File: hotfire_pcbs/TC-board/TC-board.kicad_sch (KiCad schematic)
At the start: 14 parts, among them J1 JST, J2 JST, J3 PCIE-LP-01-01-F-DV-A-TR, U1 MAX31856_Breakout, U2 MAX31856_Breakout

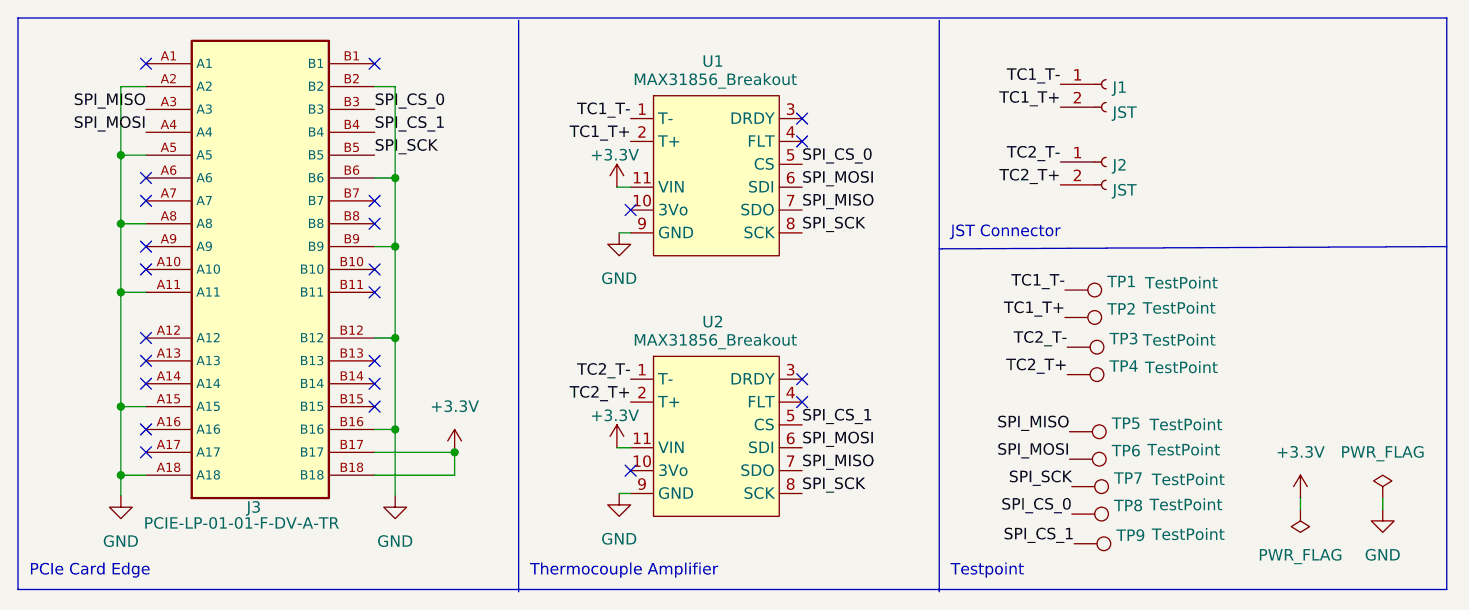
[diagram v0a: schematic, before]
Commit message: Changed JST to DSUB
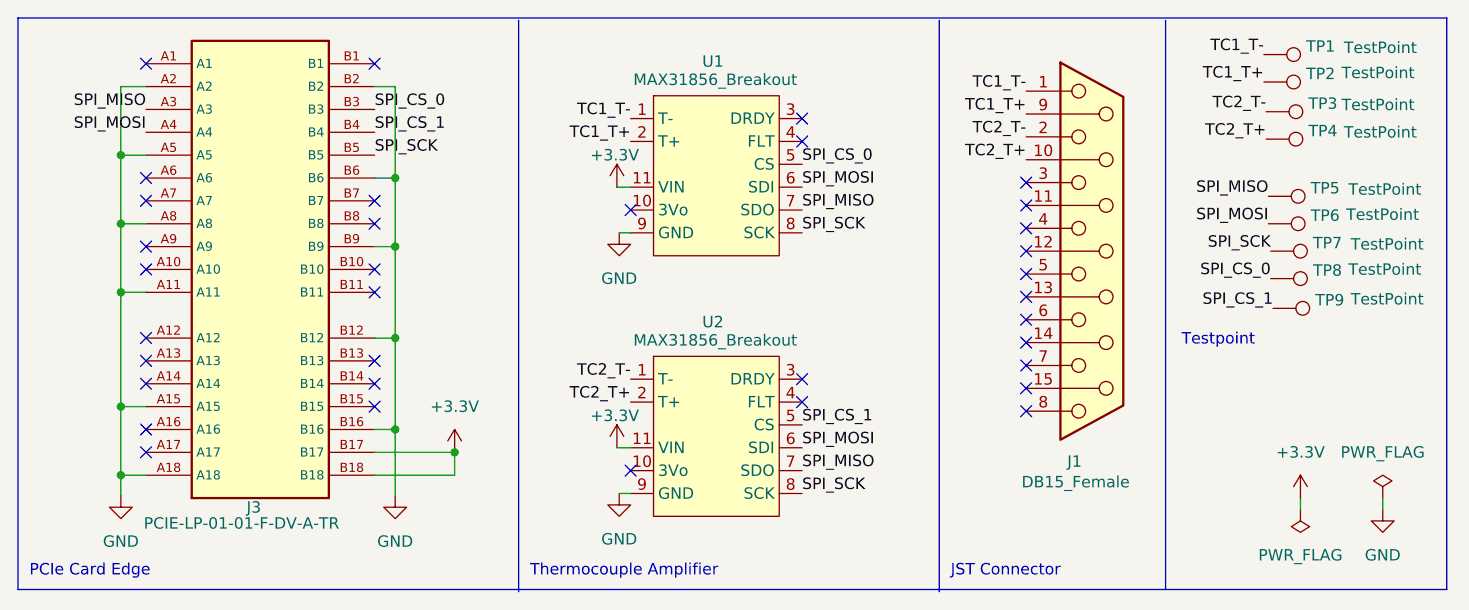
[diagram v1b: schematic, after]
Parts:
- removed J1, J2: JST, Connector_PinHeader_2.54mm:PinHeader_1x02_P2.54mm_Horizontal, symbol Connector:Conn_01x02_Female
- added J1: DB15_Female, DSUB_622-015-260-042:DSUB_622-015-260-042, symbol Connector:DB15_Female
- TP1, TP2, TP3, TP4, TP5, TP6, TP7, TP8, TP9: footprint TestPoint:TestPoint_Plated_Hole_D2.0mm -> TestPoint:TestPoint_Keystone_5010-5014_Multipurpose
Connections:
- net TC1_T+: now also J1.9 (P9)
- net TC1_T-: now also J1.1
- net TC2_T+: now also J1.10 (P10)
- net TC2_T-: now also J1.2
- net +3V3 renamed +3.3V
- no-connect marks 24 -> 35
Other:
- moved on the sheet: TP1, TP2, TP3, TP4, TP5, TP6, TP7, TP8, TP9
